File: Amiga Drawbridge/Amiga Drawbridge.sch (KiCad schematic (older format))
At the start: 17 parts, among them J1 FDC, J2 PWR_EXT1, J3 PWR_DRV, J4 PWR_EXT2, M1 Mounting, M2 Mounting, M3 Mounting, M4 Mounting

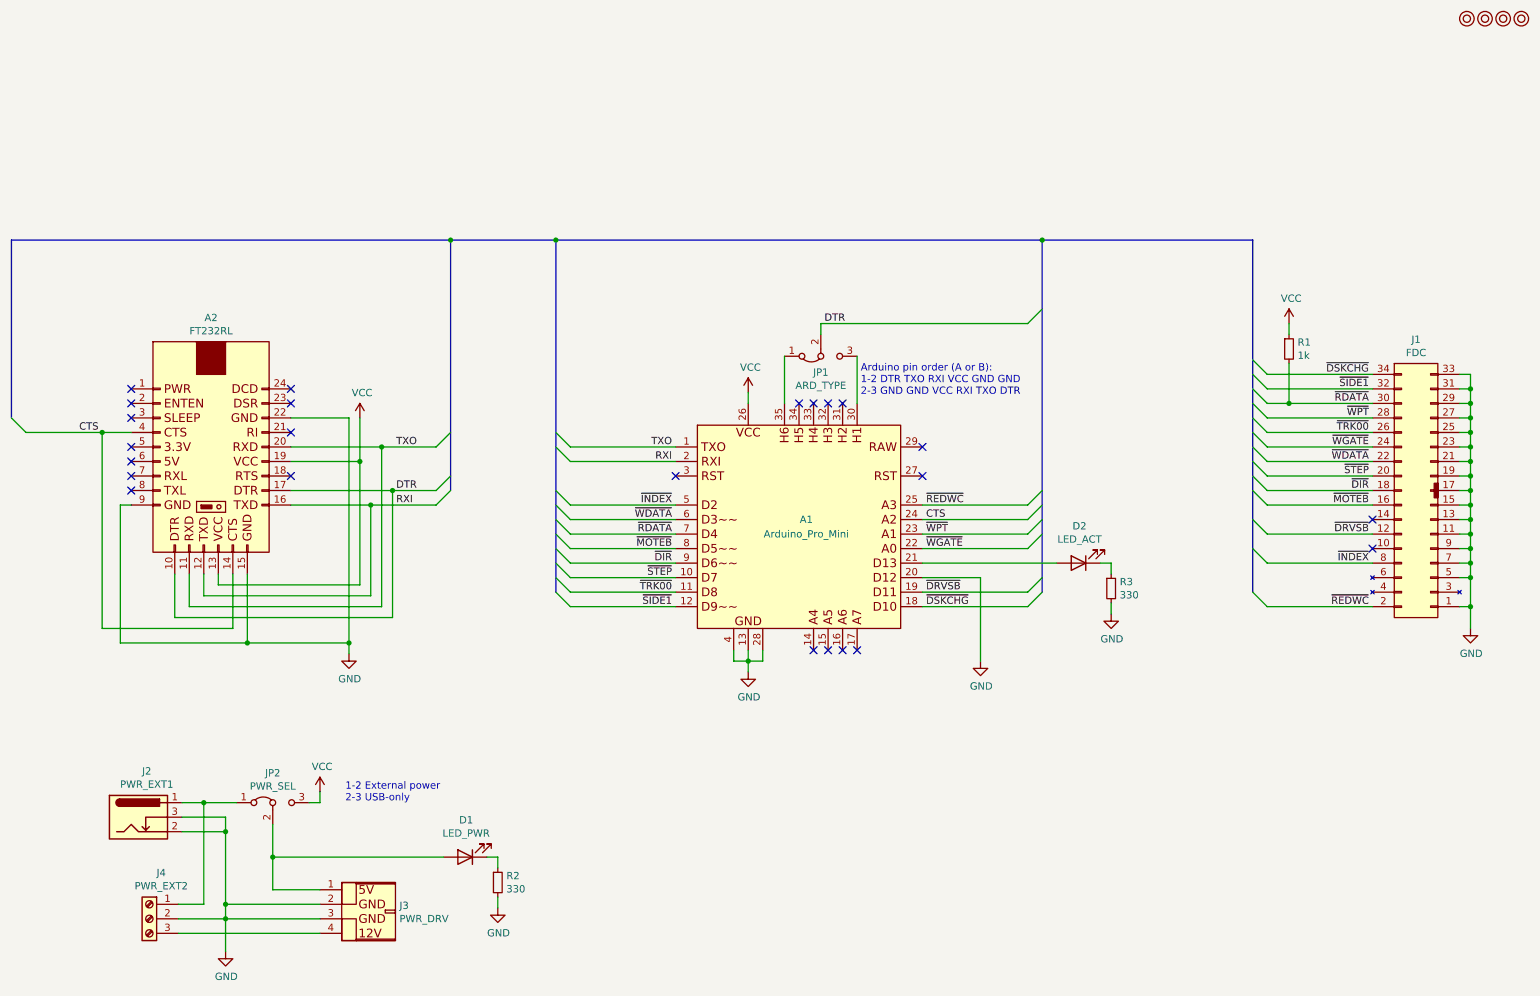
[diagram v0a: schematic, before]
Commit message: Can swap D4 and D8
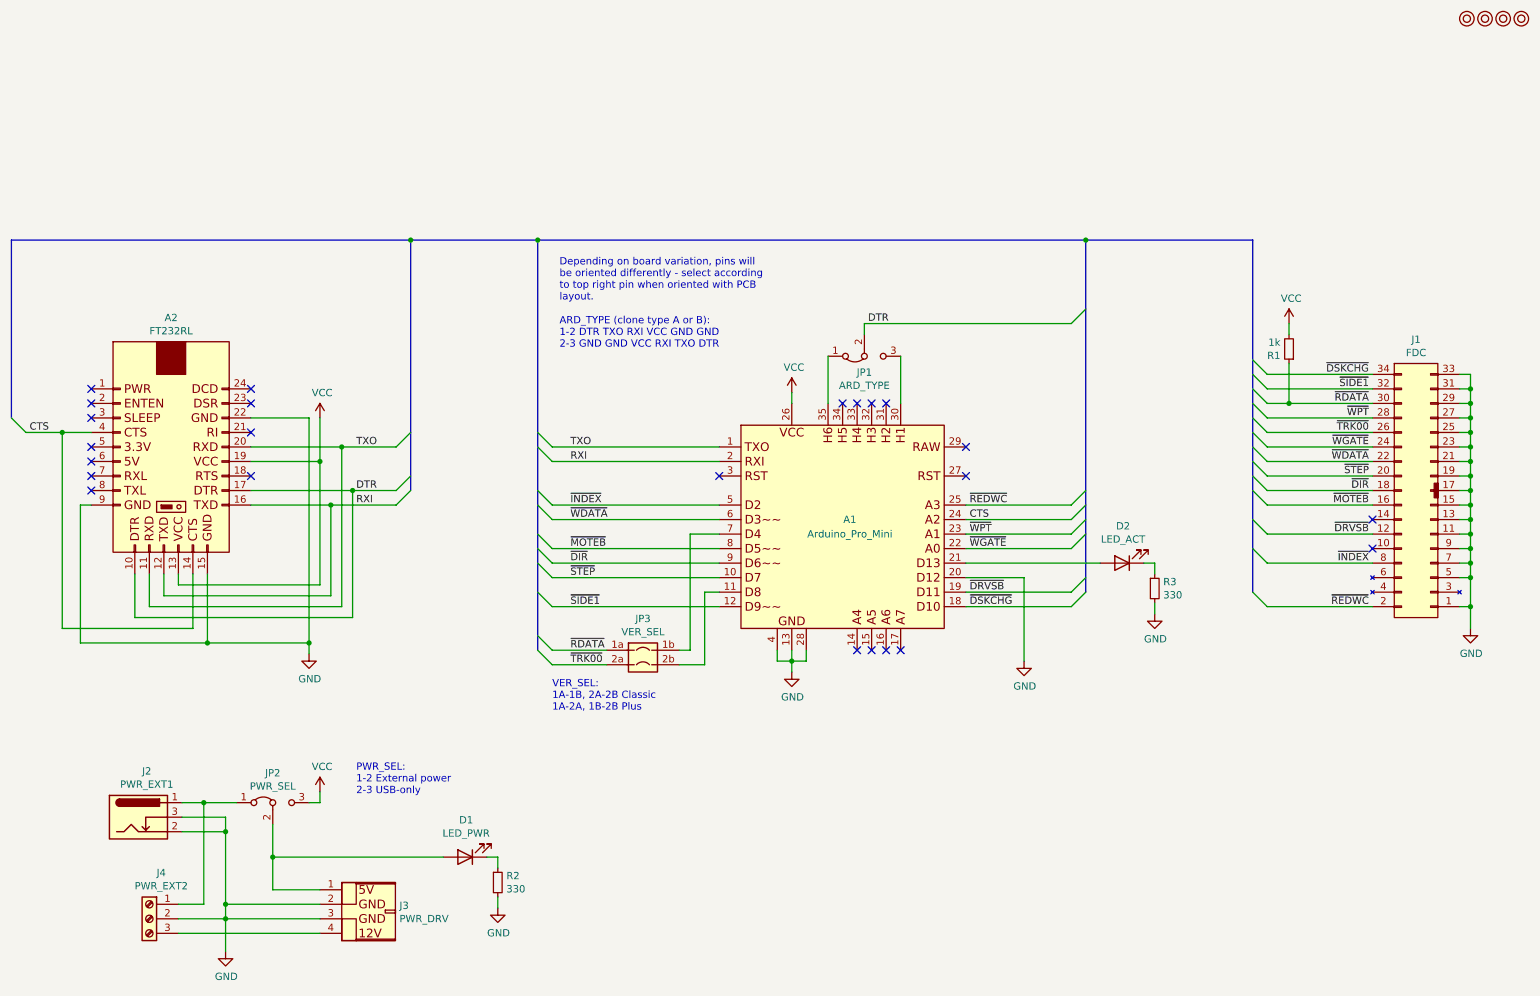
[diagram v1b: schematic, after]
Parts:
- added JP3: VER_SEL, solder_bridge:select_swappable, symbol solder_select:Jumper_4_Swappable
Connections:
- net VCC: now also R1.2; no longer R1.1
- net ~RDATA: now also R1.1, JP3.1a (Pin_1a); no longer A1.7 (D4), R1.2
- net ~TRK00: now also JP3.2a (Pin_2a); no longer A1.11 (D8)
- new net: A1.11 (D8), JP3.2b (Pin_2b)
- new net: A1.7 (D4), JP3.1b (Pin_1b)
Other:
- note added: "ARD_TYPE (clone type A or B):\n1-2 DTR TXO RXI VCC GND GND\n2-3 GND GND VCC RXI TXO DTR"
- note added: "Depending on board variation, pins will\nbe oriented differently - select according\nto top right pin when oriented with PCB\nlayout."
- note added: "PWR_SEL:\n1-2 External power\n2-3 USB-only"
- note added: "VER_SEL:\n1A-1B, 2A-2B Classic\n1A-2A, 1B-2B Plus"
- note removed: "1-2 External power\n2-3 USB-only"
- note removed: "Arduino pin order (A or B):\n1-2 DTR TXO RXI VCC GND GND\n2-3 GND GND VCC RXI TXO DTR"
- moved on the sheet: A1, A2, D2, JP1, R3

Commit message: PWR_EXT2 renamed PWR_IN2, now 4 pin to match greaseweazle
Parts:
- J2: value PWR_EXT1 -> PWR_IN1
- J4: value PWR_EXT2 -> PWR_IN2; footprint pwr_drv:PWR_EXT -> pwr_drv:PWR_IN; symbol Connector:Screw_Terminal_01x03 -> floppy:Power_Input
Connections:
- net GND: now also J4.3 (Pin_3)
- net at J2.1, JP2.1 (A): now also J4.4 (Pin_4); no longer J4.1 (Pin_1)
- net at J3.4 (Pin_4): now also J4.1 (Pin_1); no longer J4.3 (Pin_3)
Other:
- note added: "Depending on board variation, pins will\nbe oriented differently - select according\nto top right pin when overlaid PCB layout."
- note removed: "Depending on board variation, pins will\nbe oriented differently - select according\nto top right pin when oriented with PCB\nlayout."
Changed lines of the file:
@@
 P 1600 6075
 F 0 "J2" H 1657 6392 50  0000 C CNN
-F 1 "PWR_EXT1" H 1657 6301 50  0000 C CNN
+F 1 "PWR_IN1" H 1657 6301 50  0000 C CNN
 F 2 "Connector_BarrelJack:BarrelJack_Horizontal" H 1650 6035 50  0001 C CNN
 F 3 "~" H 1650 6035 50  0001 C CNN
@@
 	2200 6775 2200 7000
 $Comp
-L Connector:Screw_Terminal_01x03 J4
+L floppy:Power_Input J4
 U 1 1 61628176
 P 1675 6775
 F 0 "J4" H 1593 7092 50  0000 C CNN
-F 1 "PWR_EXT2" H 1593 7001 50  0000 C CNN
-F 2 "pwr_drv:PWR_EXT" H 1675 6775 50  0001 C CNN
+F 1 "PWR_IN2" H 1593 7001 50  0000 C CNN
+F 2 "pwr_drv:PWR_IN" H 1675 6775 50  0001 C CNN
 F 3 "~" H 1675 6775 50  0001 C CNN
 	1    1675 6775
-	-1   0    0    -1
+	-1   0    0    1
 $EndComp
 Wire Wire Line
@@
 Wire Wire Line
 	1900 6175 2200 6175
-Wire Wire Line
-	1875 6675 2050 6675
-Wire Wire Line
-	2050 6675 2050 5975
 Connection ~ 2050 5975
 Wire Wire Line
@@
 	4450 4225 5600 4225
 Text Notes 4500 2525 0    50   ~ 0
-Depending on board variation, pins will\nbe oriented differently - select according\nto top right pin when oriented with PCB\nlayout.
+Depending on board variation, pins will\nbe oriented differently - select according\nto top right pin when overlaid PCB layout.
 Text Notes 4500 2850 0    50   ~ 0
 ARD_TYPE (clone type A or B):\n1-2 DTR TXO RXI VCC GND GND\n2-3 GND GND VCC RXI TXO DTR
 Text Notes 4450 5350 0    50   ~ 0
 VER_SEL:\n1A-1B, 2A-2B Classic\n1A-2A, 1B-2B Plus
+Wire Wire Line
+	1875 6575 2050 6575
+Wire Wire Line
+	2050 6575 2050 5975
+Wire Wire Line
+	1875 6675 2200 6675
 Wire Bus Line
 	3475 2100 3475 3825

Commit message: Added asterisk
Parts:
- R2, R3: value 330 -> 330*
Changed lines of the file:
@@
 P 4075 6525
 F 0 "R2" H 4134 6571 50  0000 L CNN
-F 1 "330" H 4134 6480 50  0000 L CNN
+F 1 "330*" H 4134 6480 50  0000 L CNN
 F 2 "Resistor_THT:R_Axial_DIN0207_L6.3mm_D2.5mm_P10.16mm_Horizontal" H 4075 6525 50  0001 C CNN
 F 3 "~" H 4075 6525 50  0001 C CNN
@@
 P 8600 4500
 F 0 "R3" H 8659 4546 50  0000 L CNN
-F 1 "330" H 8659 4455 50  0000 L CNN
+F 1 "330*" H 8659 4455 50  0000 L CNN
 F 2 "Resistor_THT:R_Axial_DIN0207_L6.3mm_D2.5mm_P10.16mm_Horizontal" H 8600 4500 50  0001 C CNN
 F 3 "~" H 8600 4500 50  0001 C CNN
